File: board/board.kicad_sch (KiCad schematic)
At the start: 15 parts

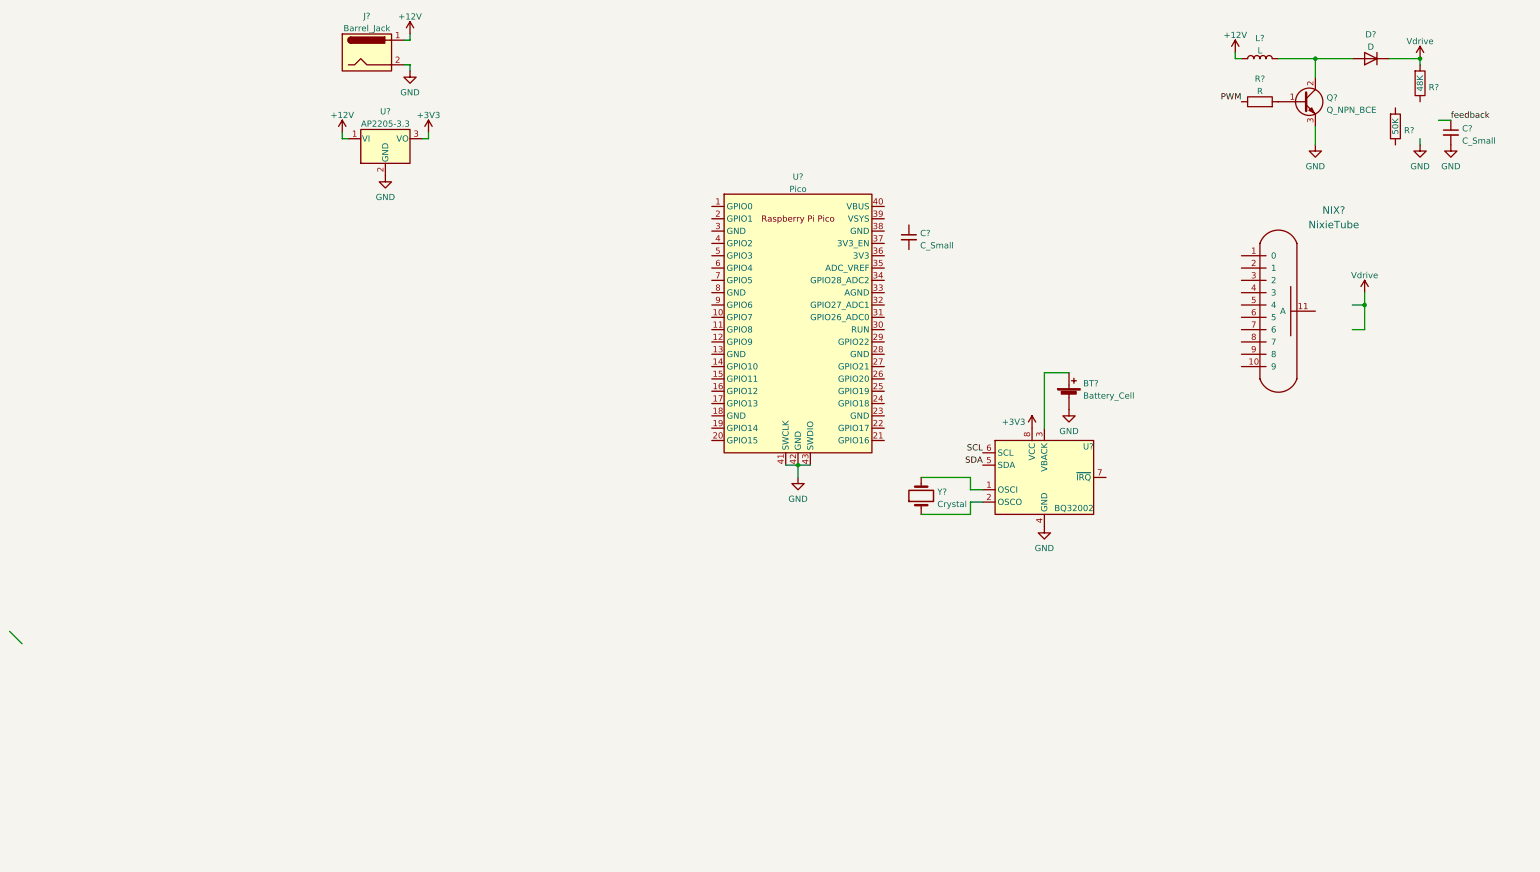
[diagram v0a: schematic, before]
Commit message: Finish schematics sans analog display circuitry.
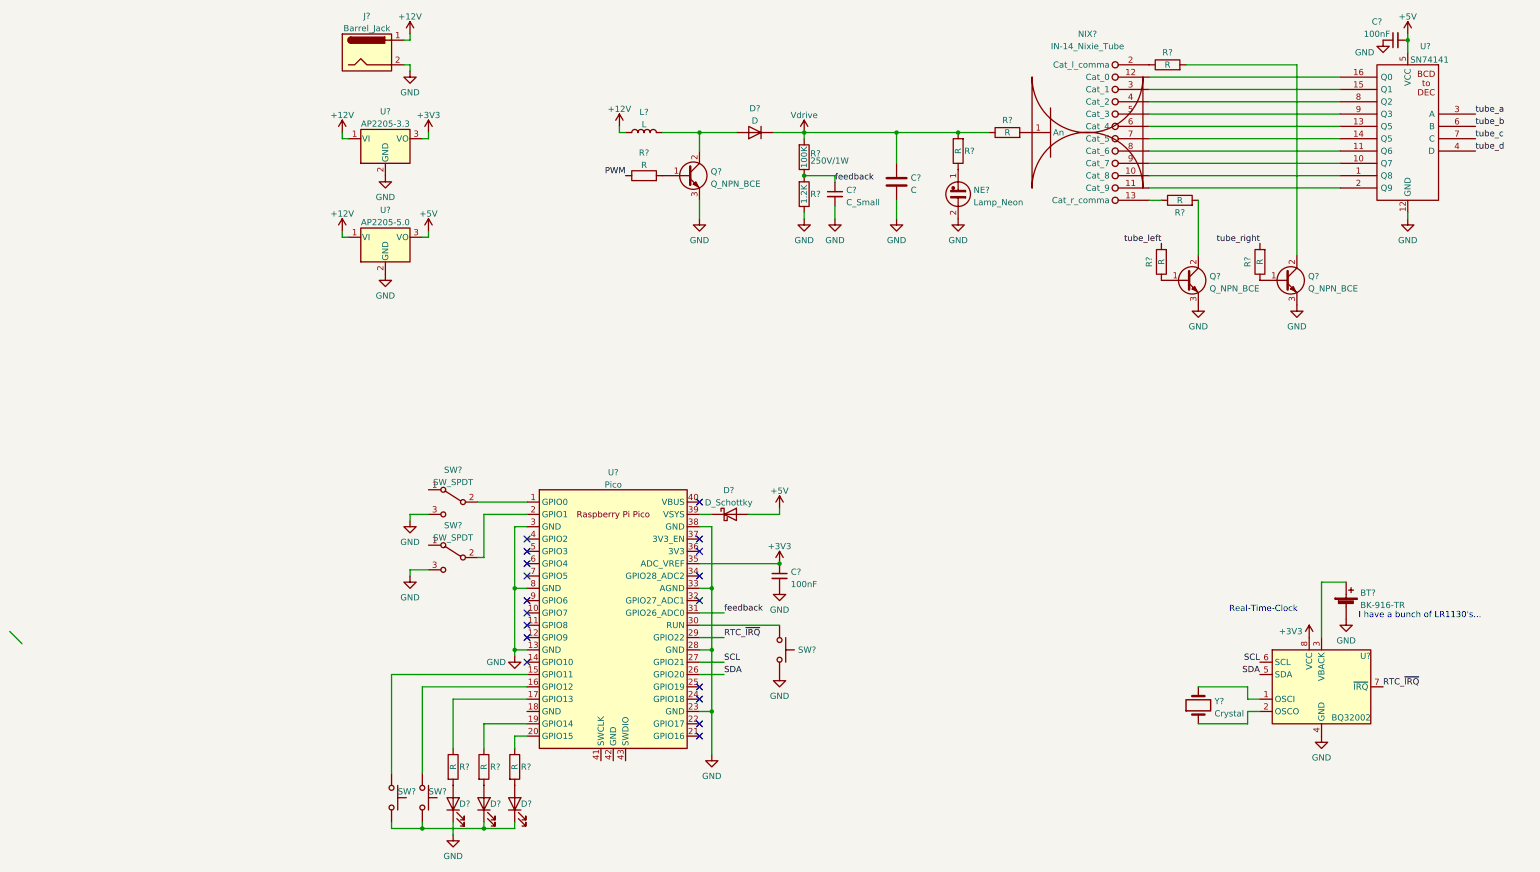
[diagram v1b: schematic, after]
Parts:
- removed NIX?: NixieTube, symbol nixie:NixieTube
- added C?: C, symbol Device:C
- added C?: 100nF, symbol Device:C_Small
- added D? (x3): LED, symbol Device:LED
- added D?: D_Schottky, symbol Device:D_Schottky
- added NE?: Lamp_Neon, symbol Device:Lamp_Neon
- added NIX?: IN-14_Nixie_Tube, symbol board:IN-14_Nixie_Tube
- added Q? (x2): Q_NPN_BCE, symbol Device:Q_NPN_BCE
- added R? (x9): R, symbol Device:R
- added SW? (x3): SW_Push, symbol Switch:SW_Push
- added SW? (x2): SW_SPDT, symbol Switch:SW_SPDT
- added U?: SN74141, Package_DIP:DIP-16_W7.62mm, symbol board:SN74141
- added U?: AP2205-5.0, Package_TO_SOT_SMD:SOT-89-3, symbol board:AP2205
- BT?: value Battery_Cell -> BK-916-TR
- C?: value C_Small -> 100nF
- R?: value 48K -> 100K; Value2 (none) -> 250V/1W
- R?: value 50K -> 1.2K
- U?: symbol board:AP2205-3.3 -> board:AP2205
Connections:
- net +12V: now also U?.1 (VI)
- net +3V3: now also C?.1, U?.35 (ADC_VREF)
- net GND: now also C?.2, R?.1, U?.13 (GND), U?.23 (GND), U?.28 (GND), U?.3 (GND), U?.33 (AGND), U?.38 (GND), U?.8 (GND), C?.1, C?.2, D?.1 (K), NE?.2, Q?.3 (E), Q?.3 (E), SW?.2, SW?.3 (C), SW?.3 (C), U?.12 (GND), U?.2 (GND); no longer U?.41 (SWCLK), U?.42 (GND), U?.43 (SWDIO)
- net SCL: now also U?.27 (GPIO21)
- net SDA: now also U?.26 (GPIO20)
- net Vdrive: now also C?.1, R?.1, R?.2
- net feedback: now also R?.1, R?.2, U?.31 (GPIO26_ADC0)
- net RTC_~{IRQ}: now reaches U?.7 (~{IRQ})
- net RTC_~{IRQ}: now also U?.29 (GPIO22)
- net at U?.1 (GPIO0): now also SW?.2 (B)
- net at U?.15 (GPIO11): now also SW?.1
- net at U?.16 (GPIO12): now also SW?.1
- net at U?.17 (GPIO13): now also R?.1
- net at U?.19 (GPIO14): now also R?.1
- net at U?.2 (GPIO1): now also SW?.2 (B)
- net at U?.20 (GPIO15): now also R?.1
- net at U?.30 (RUN): now also SW?.1
- net at U?.39 (VSYS): now also D?.1 (K)
- new net: Q?.1 (B), R?.1 (x2)
- new net: Q?.2 (C), R?.2 (x2)
- new net: D?.1 (K), D?.1 (K), SW?.2, SW?.2
- new net: D?.2 (A), R?.2 (x3)
- new net: NE?.1, R?.1
- new net: NIX?.13 (Cat_r_comma), R?.1
- new net: NIX?.1 (An), R?.2
- new net: NIX?.10 (Cat_8), U?.1 (Q8)
- new net: NIX?.11 (Cat_9), U?.2 (Q9)
- new net: NIX?.12 (Cat_0), U?.16 (Q0)
- new net: NIX?.2 (Cat_l_comma), R?.1
- new net: NIX?.3 (Cat_1), U?.15 (Q1)
- new net: NIX?.4 (Cat_2), U?.8 (Q2)
- new net: NIX?.5 (Cat_3), U?.9 (Q3)
- new net: NIX?.6 (Cat_4), U?.13 (Q5)
- new net: NIX?.7 (Cat_5), U?.14 (Q5)
- new net: NIX?.8 (Cat_6), U?.11 (Q6)
- new net: NIX?.9 (Cat_7), U?.10 (Q7)
- new net +5V: C?.2, D?.2 (A), U?.3 (VO), U?.5 (VCC)
- new net tube_a: U?.3 (A)
- new net tube_b: U?.6 (B)
- new net tube_c: U?.7 (C)
- new net tube_d: U?.4 (D)
- new net tube_left: R?.2
- new net tube_right: R?.2
- no-connect marks 0 -> 18
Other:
- note added: "I have a bunch of LR1130's..."
- note added: "Real-Time-Clock"
- company: (none) -> Daniel Indictor and Dominick Villamor
- moved on the sheet: BT?, C?, D?, L?, Q?, R?, U?, Y?
